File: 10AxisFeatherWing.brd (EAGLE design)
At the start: 50.8 x 22.9 mm, 21 parts, among them U1 BNO055, U2 BME280, Y1 32.768kHz

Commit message: Fixed IMU VDDIO not connected
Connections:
- removed net VDDIO: U1.28
- net 3.3V: now also U1.28
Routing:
- net 3.3V: track 66.9 -> 70.9 mm
- removed copper zone on layer 16, net GND
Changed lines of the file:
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@@
 <signals>
 <signal name="GND">
-<polygon width="0.254" layer="16">
-<vertex x="0" y="22.86"/>
-<vertex x="50.8" y="22.86"/>
-<vertex x="50.8" y="0"/>
-<vertex x="0" y="0"/>
-</polygon>
 <contactref element="MS1" pad="4"/>
 <contactref element="JP1" pad="13"/>
@@
 <wire x1="8.89" y1="3.81" x2="8.89" y2="1.27" width="0.254" layer="1"/>
 </signal>
-<signal name="VDDIO">
-<contactref element="U1" pad="28"/>
-</signal>
 <signal name="3.3V">
 <contactref element="U1" pad="3"/>
@@
 <wire x1="39.37" y1="13.462" x2="39.37" y2="10.668" width="0.254" layer="1"/>
 <wire x1="36.576" y1="16.256" x2="39.37" y2="13.462" width="0.254" layer="1"/>
-<wire x1="26.67" y1="16.256" x2="36.576" y2="16.256" width="0.254" layer="1"/>
-<wire x1="26.416" y1="16.002" x2="26.67" y2="16.256" width="0.254" layer="1"/>
+<wire x1="26.748" y1="16.256" x2="36.576" y2="16.256" width="0.254" layer="1"/>
 <wire x1="41.91" y1="10.414" x2="41.91" y2="10.58" width="0.254" layer="1"/>
-<wire x1="26.416" y1="16.002" x2="26.25" y2="15.875" width="0.254" layer="1"/>
+<wire x1="26.748" y1="16.256" x2="26.25" y2="15.875" width="0.254" layer="1"/>
 <wire x1="20.32" y1="13.716" x2="16.256" y2="13.716" width="0.254" layer="16"/>
 <via x="23.114" y="7.874" extent="1-16" drill="0.5"/>
@@
 <via x="39.37" y="10.668" extent="1-16" drill="0.5"/>
 <via x="16.256" y="13.716" extent="1-16" drill="0.5"/>
+<contactref element="U1" pad="28"/>
+<wire x1="27.336775" y1="13.2248" x2="27.5302" y2="13.418225" width="0.254" layer="1"/>
+<wire x1="27.5302" y1="13.418225" x2="27.5302" y2="15.211775" width="0.254" layer="1"/>
+<wire x1="26.9625" y1="13.18" x2="27.0073" y2="13.2248" width="0.254" layer="1"/>
+<wire x1="27.0073" y1="13.2248" x2="27.336775" y2="13.2248" width="0.254" layer="1"/>
+<wire x1="27.5302" y1="15.211775" x2="26.866975" y2="15.875" width="0.254" layer="1"/>
+<wire x1="26.25" y1="15.875" x2="26.866975" y2="15.875" width="0.254" layer="1"/>
 </signal>
 <signal name="CAP">

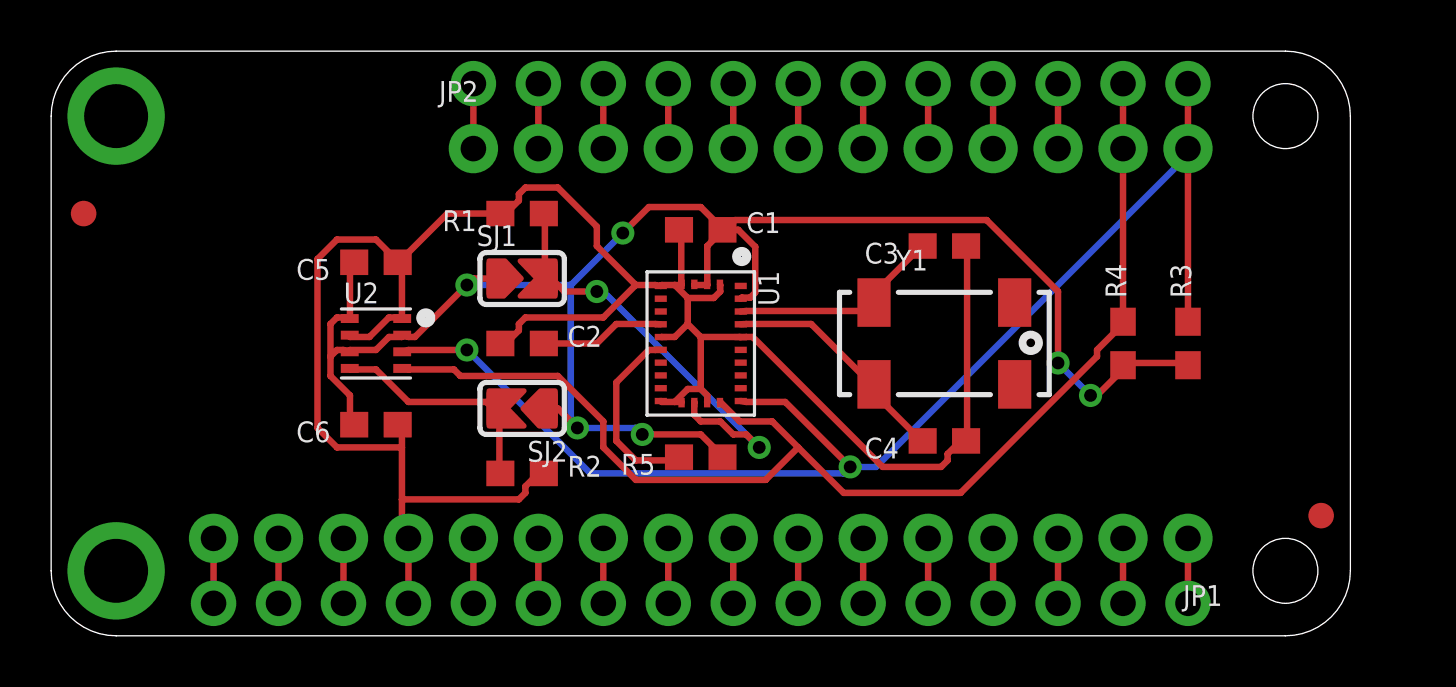
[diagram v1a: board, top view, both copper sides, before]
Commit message: Added new features
Added RESET button, INT breakout, and silk text.
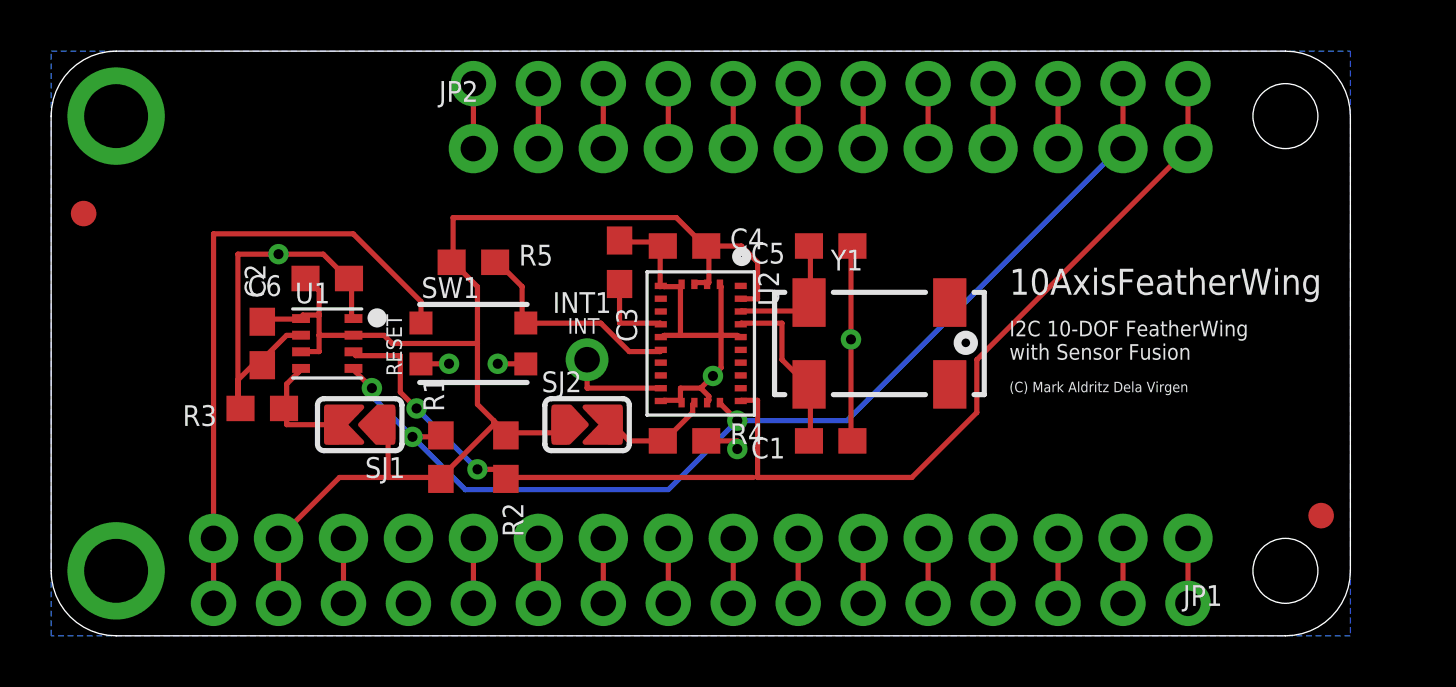
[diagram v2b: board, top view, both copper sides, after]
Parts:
- added INT1: (no value), microbuilder:1X01_ROUND
- added SW1: KMR2, microbuilder:BTN_KMR2_4.6X2.8
- C1, C5: value 0.1uF -> 22uF
- C3, C4: value 22uF -> 0.1uF
- U1: value BNO055 -> BME280; device microbuilder:BNO055 -> microbuilder:BME280
- U2: value BME280 -> BNO055; device microbuilder:BME280 -> microbuilder:BNO055
- moved R3 36.3 mm to (8.26, 8.89), turned to 180 degrees
- moved C5 17.8 mm to (30.5, 15.2)
- moved R4 17.6 mm to (24.8, 7.62), turned to 0 degrees
- moved U1 14.6 mm to (10.8, 11.4), turned to 0 degrees
- moved C3 12.7 mm to (22.2, 14.6), turned to 270 degrees
- moved U2 12.7 mm to (25.4, 11.4), turned to 270 degrees
- moved C4 12.7 mm to (24.8, 15.2), turned to 0 degrees
- moved R5 11.7 mm to (16.5, 14.6), turned to 0 degrees
- moved C2 10.2 mm to (8.26, 11.4), turned to 90 degrees
- moved R1 10.0 mm to (15.2, 6.99), turned to 90 degrees
- moved C1 9.69 mm to (30.5, 7.62), turned to 180 degrees
- moved SJ1 8.54 mm to (12.1, 8.26), turned to 180 degrees
- moved C6 6.02 mm to (10.8, 14.0)
- moved SJ2 2.62 mm to (21.0, 8.26), turned to 0 degrees
- moved Y1 2.54 mm to (32.4, 11.4)
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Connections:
- removed net 3V: JP1.15, MS1.2
- net 3.3V: now also C2.2, C4.2, JP1.15, MS1.2, R1.1, R2.1, U1.2, U1.6, U1.8, U2.28, U2.3, U2.4; no longer C1.2, C5.2, R3.1, R4.1, U1.28, U1.3, U1.4, U2.2, U2.6, U2.8
- net CAP: now also C3.2, U2.9; no longer C2.2, U1.9
- net COM3: now also R4.1, SJ2.2, U2.17; no longer R1.1, SJ1.2, U1.17
- net GND: now also R3.2, R4.2, SW1.B, SW1.B', U1.1, U1.7, U2.10, U2.15, U2.16, U2.18, U2.2, U2.25, U2.5, U2.6; no longer R1.2, R2.2, U1.10, U1.15, U1.16, U1.18, U1.2, U1.25, U1.5, U1.6, U2.1, U2.7
- net INT: now also INT1.1, U2.14; no longer U1.14
- net NRESET: now also SW1.A, U2.11; no longer U1.11
- net RESET: now also SW1.A'
- net SCL: now also R1.2, U1.4, U2.19; no longer R4.2, U1.19, U2.4
- net SDA: now also R2.2, U1.3, U2.20; no longer R3.2, U1.20, U2.3
- net SDO: now also R3.1, SJ1.2, U1.5; no longer R2.1, SJ2.2, U2.5
- net XIN32: now also C5.2, U2.27; no longer C3.2, U1.27
- net XOUT32: now also C1.2, U2.26; no longer C4.2, U1.26
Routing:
- net GND: track 86.0 -> 45.1 mm, vias 0 -> 6
- net RESET: track 2.54 -> 24.5 mm
- net 3.3V: track 70.9 -> 56.4 mm, vias 6 -> 0
- net COM3: track 17.3 -> 4.25 mm, vias 2 -> 0
- net SCL: track 47.9 -> 42.5 mm, vias 0 -> 3
- net SDO: track 9.09 -> 4.37 mm
- net SDA: track 52.8 -> 48.4 mm
- net INT: track 0.00 -> 3.99 mm
- net XIN32: track 8.49 -> 5.27 mm
- net 3V: track 2.54 -> 0.00 mm
- net XOUT32: track 9.34 -> 6.80 mm
- net CAP: track 4.89 -> 3.17 mm
- net NRESET: track 7.36 -> 8.72 mm
- added copper zone on layer 16, net GND
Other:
- board text added: "(C) Mark Aldritz Dela Virgen"
- board text added: "10AxisFeatherWing"
- board text added: "I2C 10-DOF FeatherWing with Sensor Fusion"
- board text added: "INT"
- board text added: "RESET"

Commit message: Corrected crystal capacitor values
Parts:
- C1, C5: value 22uF -> 22pF
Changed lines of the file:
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@@
 <attribute name="VALUE" x="21.463" y="12.827" size="0.4064" layer="27" font="vector" ratio="10" rot="R270"/>
 </element>
-<element name="C5" library="microbuilder" package="0603-NO" value="22uF" x="30.48" y="15.24" smashed="yes" rot="R180">
+<element name="C5" library="microbuilder" package="0603-NO" value="22pF" x="30.48" y="15.24" smashed="yes" rot="R180">
 <attribute name="NAME" x="28.702" y="15.367" size="0.8128" layer="25" font="vector" ratio="18" rot="R180"/>
 <attribute name="SPICEPREFIX" value="C" x="30.48" y="15.24" size="1.778" layer="27" rot="R180" display="off"/>
 <attribute name="VALUE" x="28.702" y="16.002" size="0.4064" layer="27" font="vector" ratio="10" rot="R180"/>
 </element>
-<element name="C1" library="microbuilder" package="0603-NO" value="22uF" x="30.48" y="7.62" smashed="yes" rot="R180">
+<element name="C1" library="microbuilder" package="0603-NO" value="22pF" x="30.48" y="7.62" smashed="yes" rot="R180">
 <attribute name="NAME" x="28.702" y="7.747" size="0.8128" layer="25" font="vector" ratio="18" rot="R180"/>
 <attribute name="SPICEPREFIX" value="C" x="30.48" y="7.62" size="1.778" layer="27" rot="R180" display="off"/>
